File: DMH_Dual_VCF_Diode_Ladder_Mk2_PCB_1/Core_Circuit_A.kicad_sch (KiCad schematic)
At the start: 43 parts, among them J19 Conn_01x04_PinHeader, SW1 SW_SPDT, SW2 SW_SPDT, SW3 SW_SPDT, U3 TL074, U5 TL074

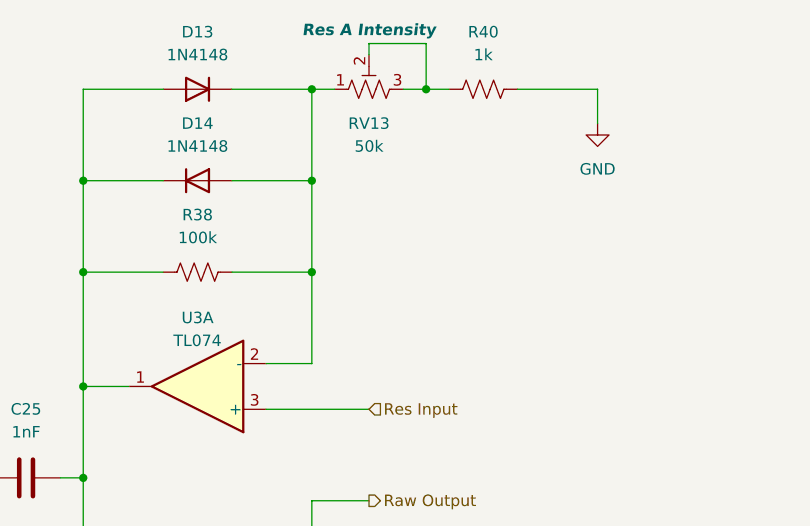
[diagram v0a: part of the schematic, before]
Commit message: Moved Res Int and CV3 V/Oct trims to front panel
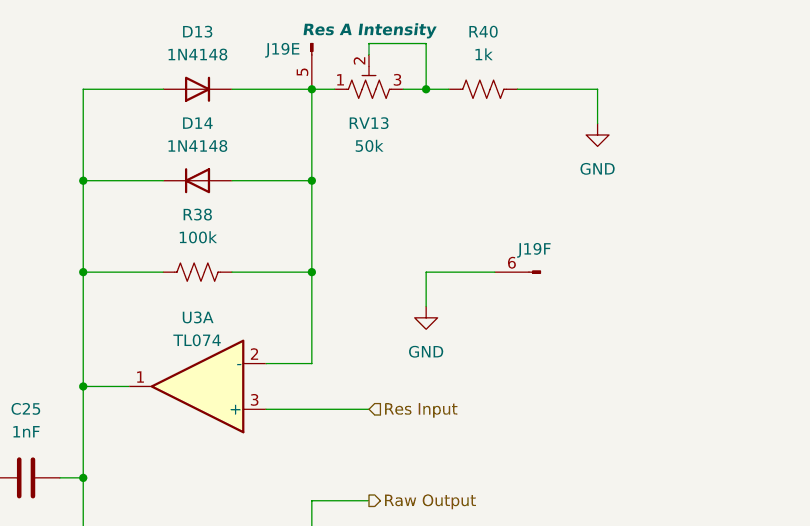
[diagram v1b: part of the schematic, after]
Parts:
- added unit 5 of J19
- added unit 6 of J19
- J19: value Conn_01x04_PinHeader -> Conn_01x06_PinHeader; footprint Connector_PinHeader_2.54mm:PinHeader_1x04_P2.54mm_Vertical -> (none); symbol SynthStuff:Conn_01x04_PinHeader -> SynthStuff:Conn_01x06_PinHeader
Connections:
- net GND: now also J19.6 (Pin_6)
- net at D13.1 (K), D14.2 (A), R38.2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: now also J19.5 (Pin_5)

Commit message: Finished Mk2.0
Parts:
- J19: footprint (none) -> Connector_PinHeader_2.54mm:PinHeader_1x06_P2.54mm_Vertical
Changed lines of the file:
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@@
 			)
 		)
-		(property "Footprint" ""
+		(property "Footprint" "Connector_PinHeader_2.54mm:PinHeader_1x06_P2.54mm_Vertical"
 			(at 146.05 81.28 0)
 			(effects
@@
 			)
 		)
-		(property "Footprint" ""
+		(property "Footprint" "Connector_PinHeader_2.54mm:PinHeader_1x06_P2.54mm_Vertical"
 			(at 203.2 25.4 0)
 			(effects
@@
 			)
 		)
-		(property "Footprint" ""
+		(property "Footprint" "Connector_PinHeader_2.54mm:PinHeader_1x06_P2.54mm_Vertical"
 			(at 74.93 41.91 0)
 			(effects
@@
 			)
 		)
-		(property "Footprint" ""
+		(property "Footprint" "Connector_PinHeader_2.54mm:PinHeader_1x06_P2.54mm_Vertical"
 			(at 228.6 50.8 0)
 			(effects
@@
 			)
 		)
-		(property "Footprint" ""
+		(property "Footprint" "Connector_PinHeader_2.54mm:PinHeader_1x06_P2.54mm_Vertical"
 			(at 134.62 114.3 0)
 			(effects
@@
 			)
 		)
-		(property "Footprint" ""
+		(property "Footprint" "Connector_PinHeader_2.54mm:PinHeader_1x06_P2.54mm_Vertical"
 			(at 88.9 69.85 0)
 			(effects
